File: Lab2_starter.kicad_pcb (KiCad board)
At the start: 4 copper layers, 121.8 x 101.6 mm, 79 parts, among them J1 973582101, J2 973582100, J3 973582101, J4 973582100, J5 Conn_01x01, J6 Conn_01x01, Q1 NMOS, Q2 NMOS, SW1 SW_Push_DPDT, U1 IR2010, U2 CT416-HSN820DR, U3 LAUNCHXL-F28P55X_BottomHalf

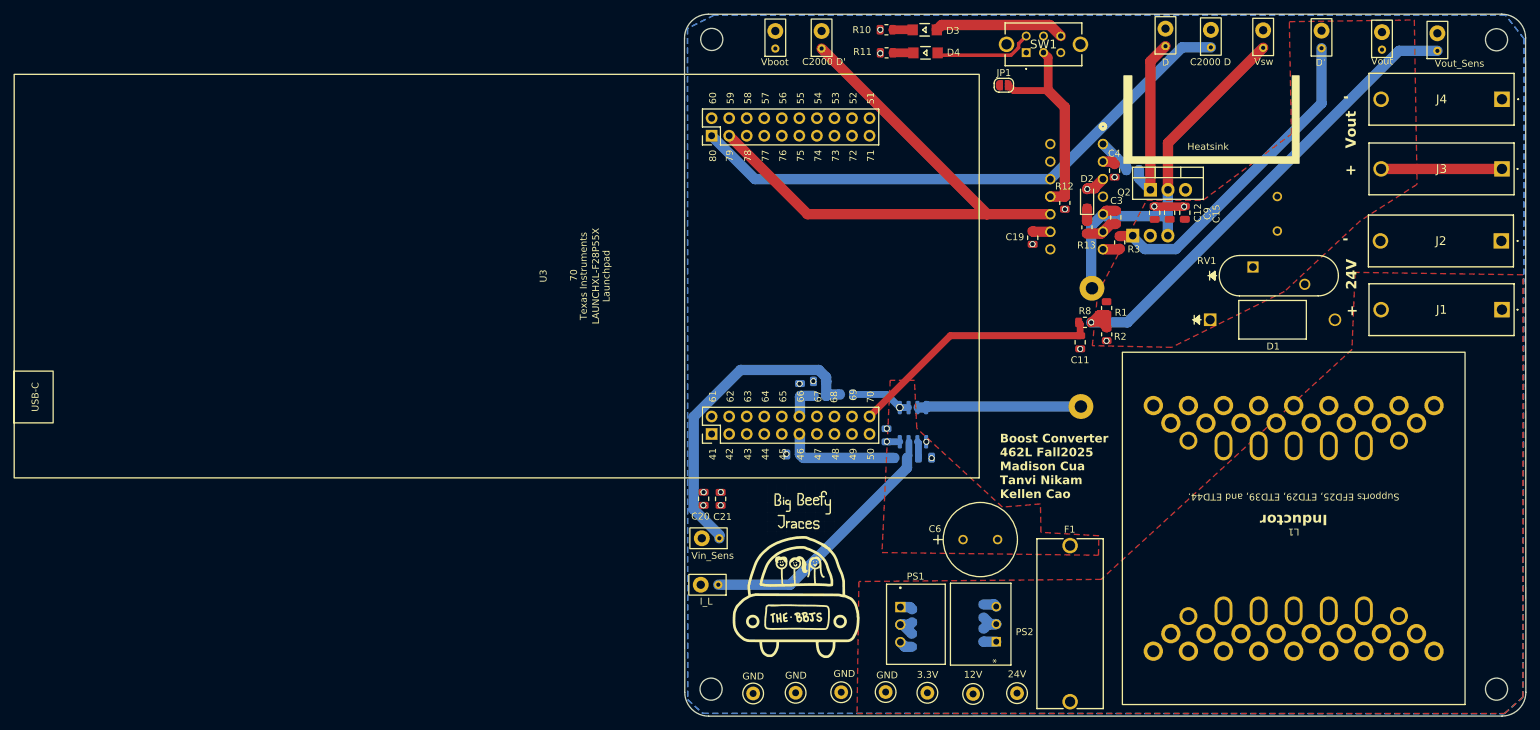
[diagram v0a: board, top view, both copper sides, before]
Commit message: Fixed Uneven copper distribution
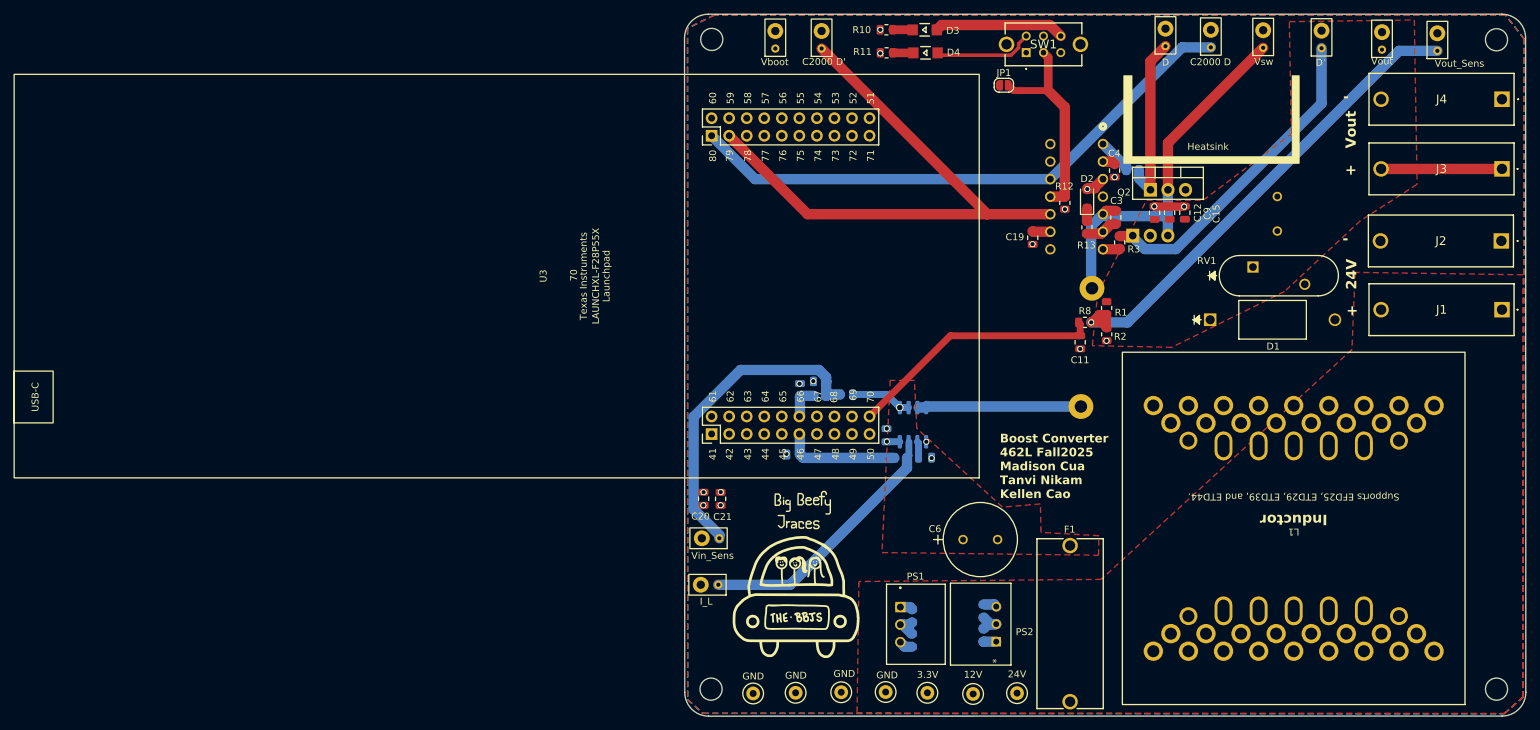
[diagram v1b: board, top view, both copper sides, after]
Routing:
- added copper zone on F.Cu, net GND
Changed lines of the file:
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@@
 		(layer "F.Cu")
 		(hatch edge 0.5)
+		(priority 1)
 		(connect_pads yes
 			(clearance 0.5)
@@
 			)
 		)
+	)
+	(zone
+		(net 2)
+		(net_name "GND")
+		(layer "F.Cu")
+		(hatch edge 0.5)
+		(connect_pads yes
+			(clearance 0.5)
+		)
+		(min_thickness 0.25)
+		(filled_areas_thickness no)
+		(fill yes
+			(thermal_gap 0.5)
+			(thermal_bridge_width 0.5)
+			(island_removal_mode 1)
+			(island_area_min 10)
+		)
+		(polygon
+			(pts
+				(xy 141.59 41.47) (xy 138.94 38.06) (xy 24.38 38.03) (xy 20.5 39.91) (xy 20.5 137.09) (xy 22.69 139.1)
+				(xy 138.76 139.13) (xy 141.42 136.77)
+			)
+		)
